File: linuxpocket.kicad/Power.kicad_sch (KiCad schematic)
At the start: 44 parts, among them U1 BQ24295RGER, U2 BQ27426YZFR, U3 TPS63805YFFR, U4 TPS61169DCKR, U5 MT3608L

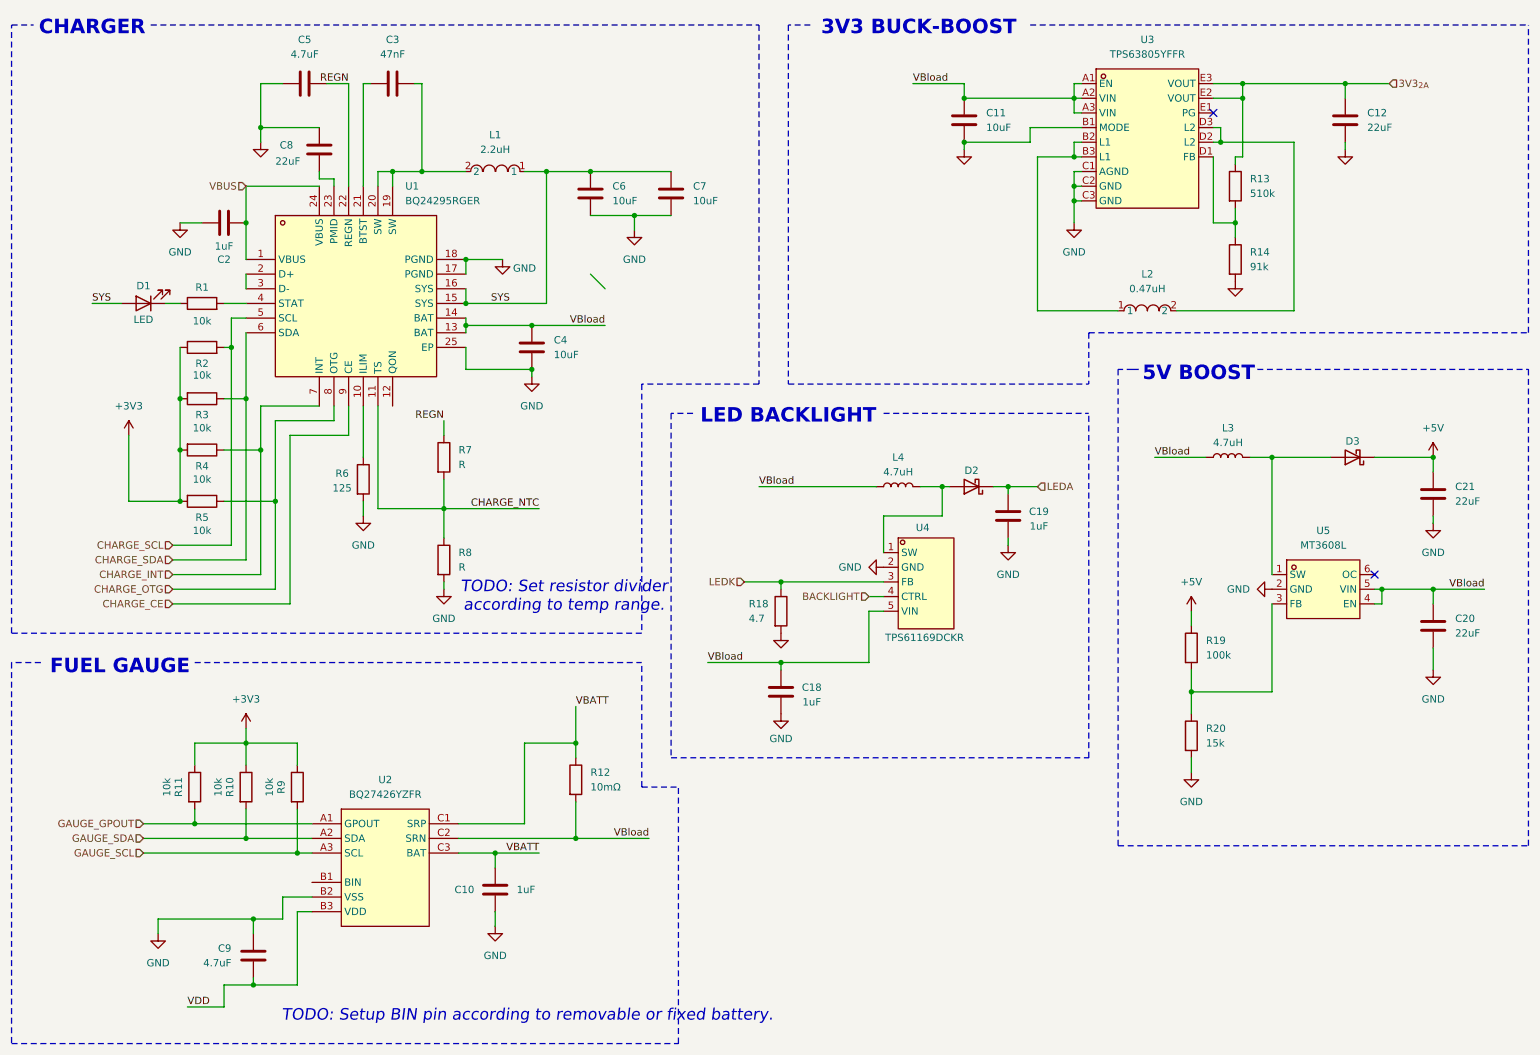
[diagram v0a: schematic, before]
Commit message: Add keyboard, improve many things etc.
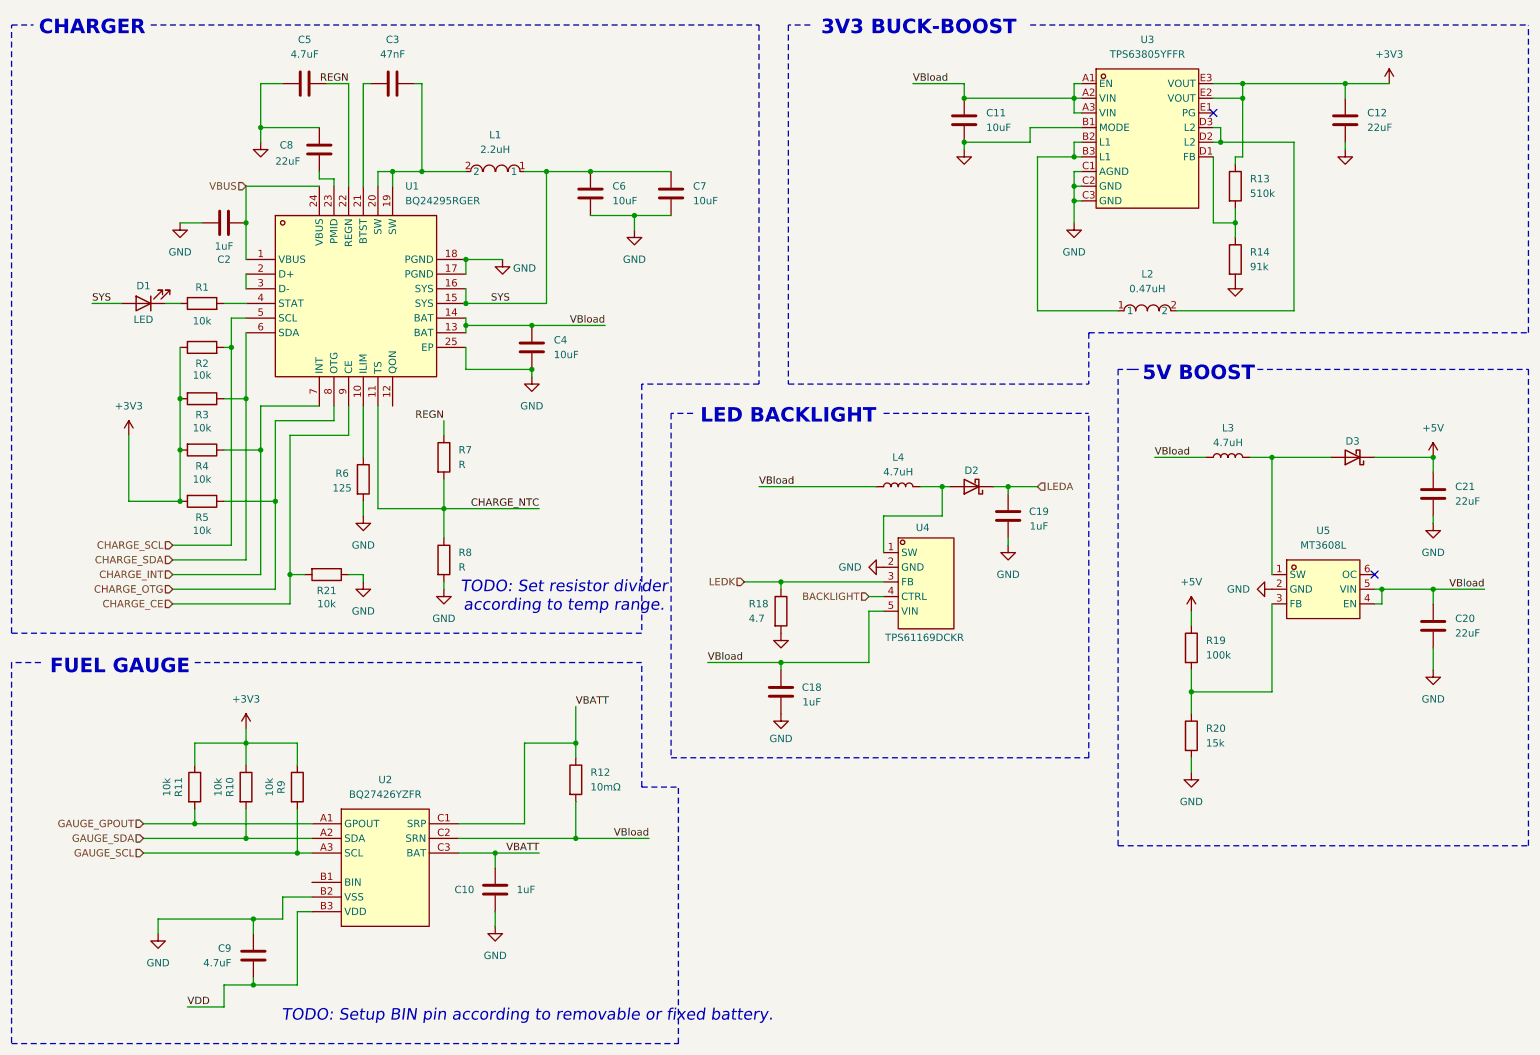
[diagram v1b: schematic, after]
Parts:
- added R21: 10k, symbol Device:R
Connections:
- net 3V3_{2A} is gone; now on net +3V3: C12.1, R13.1, U3.E2 (VOUT), U3.E3 (VOUT)
- net CHARGE_CE: now also R21.2
- net GND: now also R21.1
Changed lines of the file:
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@@
 	)
 	(junction
+		(at 64.77 113.03)
+		(diameter 0)
+		(color 0 0 0 0)
+	)
+	(junction
 		(at 109.22 43.18)
 		(diameter 0)
@@
 		(at 252.73 113.03)
 	)
-	(bus_entry
-		(at 116.84 60.96)
-		(size 2.54 2.54)
-		(stroke
-			(width 0)
-			(type default)
-		)
-	)
 	(wire
 		(pts
@@
 		)
 	)
+	(wire
+		(pts
+			(xy 77.47 113.03) (xy 77.47 114.3)
+		)
+		(stroke
+			(width 0)
+			(type default)
+		)
+	)
 	(polyline
 		(pts
@@
 	(wire
 		(pts
+			(xy 67.31 113.03) (xy 64.77 113.03)
+		)
+		(stroke
+			(width 0)
+			(type default)
+		)
+	)
+	(wire
+		(pts
 			(xy 143.51 114.3) (xy 149.86 114.3)
 		)
@@
 	(wire
 		(pts
-			(xy 64.77 88.9) (xy 64.77 118.11)
+			(xy 64.77 88.9) (xy 64.77 113.03)
 		)
 		(stroke
@@
 	(wire
 		(pts
+			(xy 64.77 113.03) (xy 64.77 118.11)
+		)
+		(stroke
+			(width 0)
+			(type default)
+		)
+	)
+	(wire
+		(pts
 			(xy 201.93 27.94) (xy 200.66 27.94)
 		)
@@
 	(wire
 		(pts
+			(xy 74.93 113.03) (xy 77.47 113.03)
+		)
+		(stroke
+			(width 0)
+			(type default)
+		)
+	)
+	(wire
+		(pts
 			(xy 189.23 106.68) (xy 189.23 107.95)
 		)
@@
 		)
 	)
-	(hierarchical_label "3V3_{2A}"
-		(shape input)
-		(at 255.27 27.94 0)
-		(fields_autoplaced yes)
-		(effects
-			(font
-				(size 1.27 1.27)
-			)
-			(justify left)
-		)
-	)
 	(hierarchical_label "CHARGE_CE"
 		(shape input)
@@
 	)
 	(symbol
+		(lib_id "power:+3V3")
+		(at 255.27 27.94 0)
+		(unit 1)
+		(exclude_from_sim no)
+		(in_bom yes)
+		(on_board yes)
+		(dnp no)
+		(fields_autoplaced yes)
+		(property "Reference" "#PWR04"
+			(at 255.27 31.75 0)
+			(effects
+				(font
+					(size 1.27 1.27)
+				)
+				(hide yes)
+			)
+		)
+		(property "Value" "+3V3"
+			(at 255.27 22.86 0)
+			(effects
+				(font
+					(size 1.27 1.27)
+				)
+			)
+		)
+		(property "Footprint" ""
+			(at 255.27 27.94 0)
+			(effects
+				(font
+					(size 1.27 1.27)
+				)
+				(hide yes)
+			)
+		)
+		(property "Datasheet" ""
+			(at 255.27 27.94 0)
+			(effects
+				(font
+					(size 1.27 1.27)
+				)
+				(hide yes)
+			)
+		)
+		(property "Description" "Power symbol creates a global label with name \"+3V3\""
+			(at 255.27 27.94 0)
+			(effects
+				(font
+					(size 1.27 1.27)
+				)
+				(hide yes)
+			)
+		)
+		(pin "1"
+		)
+		(instances
+			(project "linuxpocket"
+				(path "/de3771bf-b13a-459d-a957-6ff90f7da387/80740467-2537-4aa9-be41-8a76ad0fbd83"
+					(reference "#PWR04")
+					(unit 1)
+				)
+			)
+		)
+	)
+	(symbol
 		(lib_id "power:GND")
 		(at 149.86 123.19 0)
@@
 	(symbol
 		(lib_id "power:GND")
+		(at 77.47 114.3 0)
+		(unit 1)
+		(exclude_from_sim no)
+		(in_bom yes)
+		(on_board yes)
+		(dnp no)
+		(fields_autoplaced yes)
+		(property "Reference" "#PWR047"
+			(at 77.47 120.65 0)
+			(effects
+				(font
+					(size 1.27 1.27)
+				)
+				(hide yes)
+			)
+		)
+		(property "Value" "GND"
+			(at 77.47 119.38 0)
+			(effects
+				(font
+					(size 1.27 1.27)
+				)
+			)
+		)
+		(property "Footprint" ""
+			(at 77.47 114.3 0)
+			(effects
+				(font
+					(size 1.27 1.27)
+				)
+				(hide yes)
+			)
+		)
+		(property "Datasheet" ""
+			(at 77.47 114.3 0)
+			(effects
+				(font
+					(size 1.27 1.27)
+				)
+				(hide yes)
+			)
+		)
+		(property "Description" "Power symbol creates a global label with name \"GND\" , ground"
+			(at 77.47 114.3 0)
+			(effects
+				(font
+					(size 1.27 1.27)
+				)
+				(hide yes)
+			)
+		)
+		(pin "1"
+		)
+		(instances
+			(project "linuxpocket"
+				(path "/de3771bf-b13a-459d-a957-6ff90f7da387/80740467-2537-4aa9-be41-8a76ad0fbd83"
+					(reference "#PWR047")
+					(unit 1)
+				)
+			)
+		)
+	)
+	(symbol
+		(lib_id "power:GND")
 		(at 247.65 39.37 0)
 		(unit 1)
@@
 					(unit 1)
 				)
+			)
+		)
+	)
+	(symbol
+		(lib_id "Device:R")
+		(at 71.12 113.03 270)
+		(unit 1)
+		(exclude_from_sim no)
+		(in_bom yes)
+		(on_board yes)
+		(dnp no)
+		(property "Reference" "R21"
+			(at 71.12 115.824 90)
+			(effects
+				(font
+					(size 1.27 1.27)
+				)
+			)
+		)
+		(property "Value" "10k"
+			(at 71.12 118.11 90)
+			(effects
+				(font
+					(size 1.27 1.27)
+				)
+			)
+		)
+		(property "Footprint" ""
+			(at 71.12 111.252 90)
+			(effects
+				(font
+					(size 1.27 1.27)
+				)
+				(hide yes)
+			)
+		)
+		(property "Datasheet" "~"
+			(at 71.12 113.03 0)
+			(effects
+				(font
+					(size 1.27 1.27)
+				)
+				(hide yes)
+			)
+		)
+		(property "Description" "Resistor"
+			(at 71.12 113.03 0)
+			(effects
+				(font
+					(size 1.27 1.27)
+				)
+				(hide yes)
+			)
+		)
+		(pin "2"
+		)
+		(pin "1"
+		)
+		(instances
+			(project "linuxpocket"
+				(path "/de3771bf-b13a-459d-a957-6ff90f7da387/80740467-2537-4aa9-be41-8a76ad0fbd83"
+					(reference "R21")
+					(unit 1)
+				)

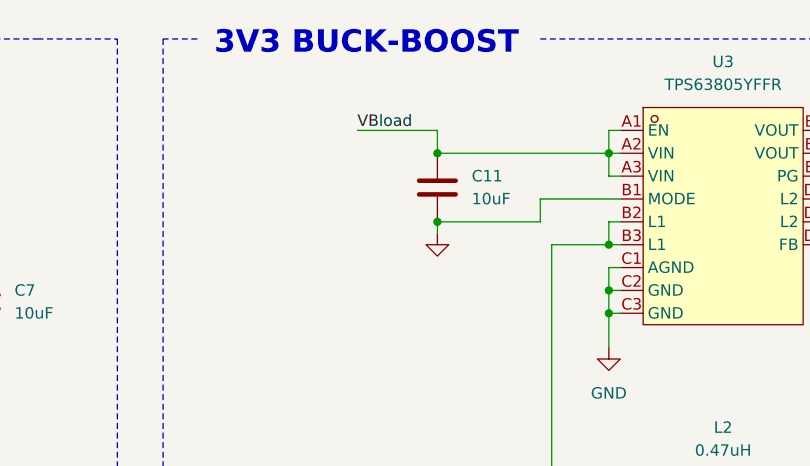
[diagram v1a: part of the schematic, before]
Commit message: Start with HDMI connector.
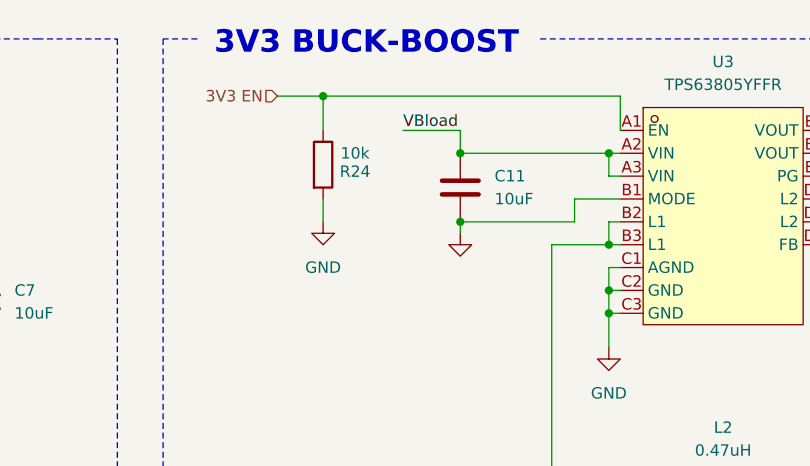
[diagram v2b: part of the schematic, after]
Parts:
- added R24: 10k, symbol Device:R
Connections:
- net GND: now also R24.2
- net VBload: no longer U3.A1 (EN)
- new net 3V3 EN: R24.1, U3.A1 (EN)
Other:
- moved on the sheet: C11

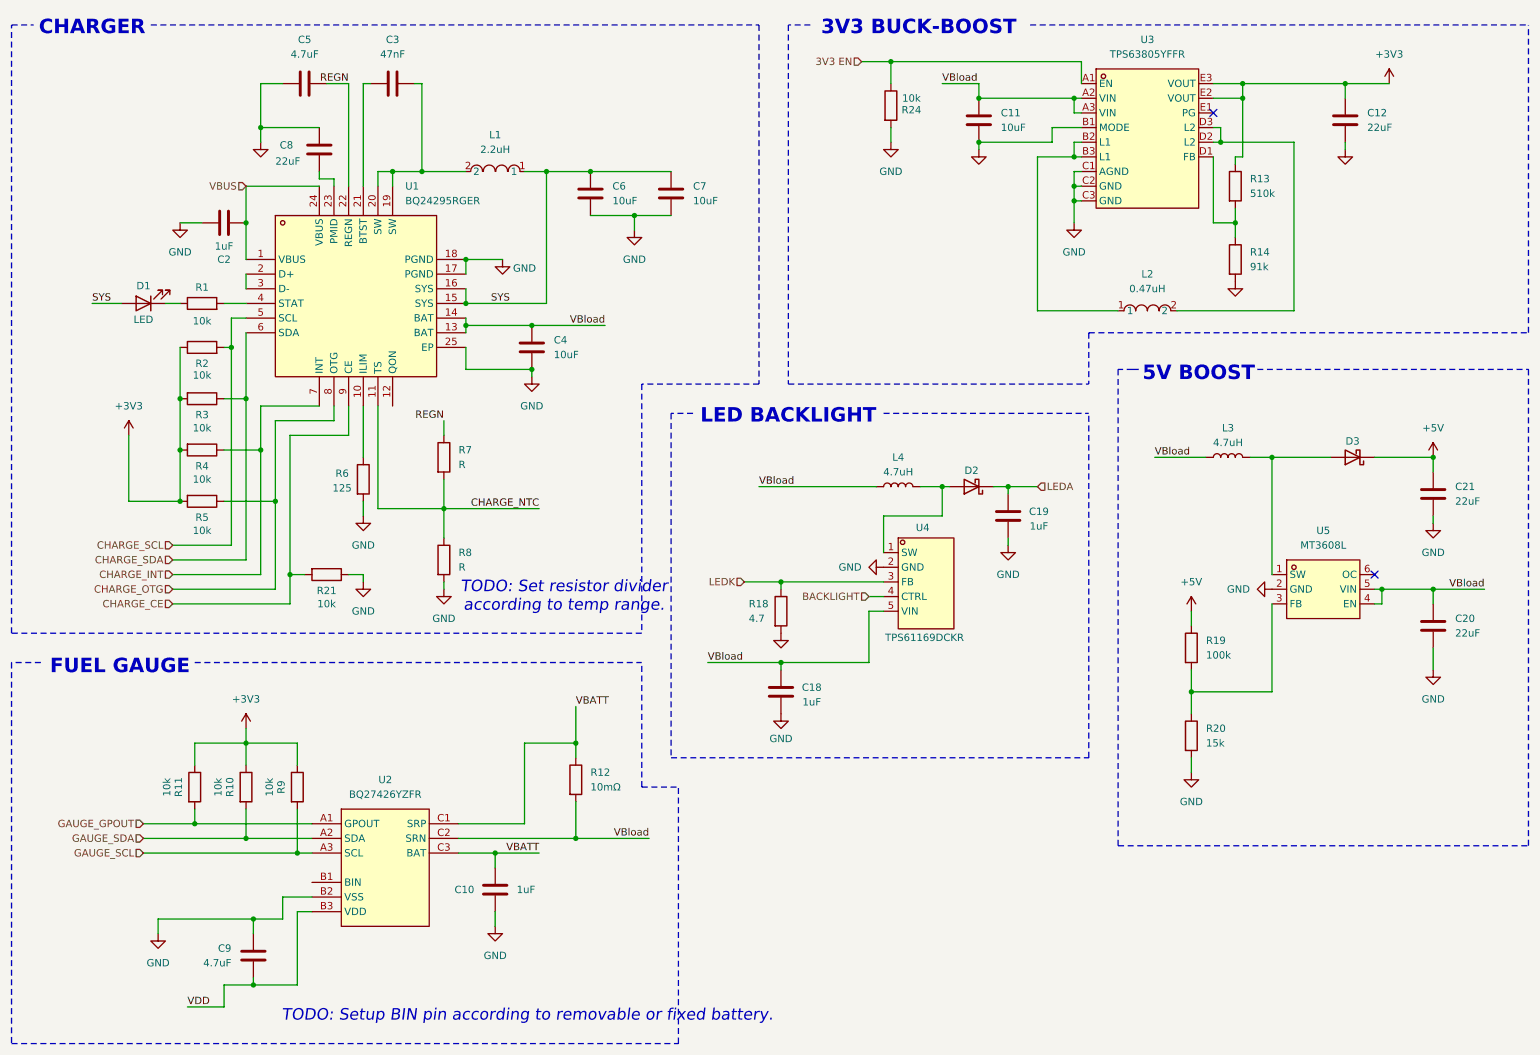
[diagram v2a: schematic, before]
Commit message: Add magnetometer #5. Add footprints to some symbols.
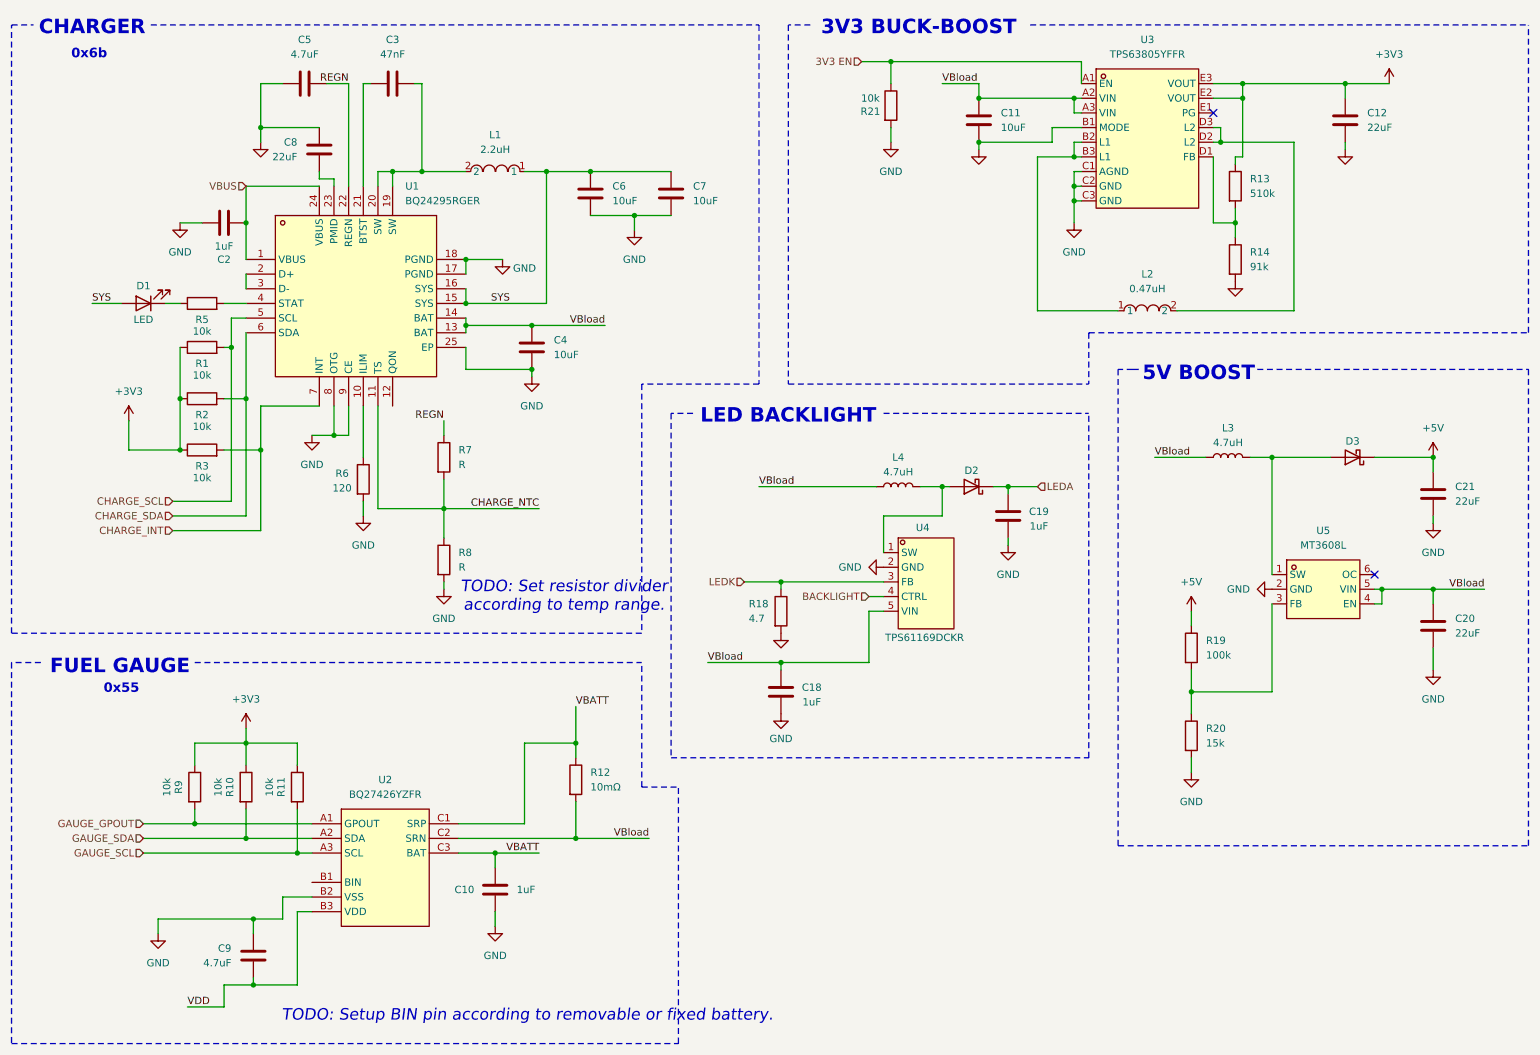
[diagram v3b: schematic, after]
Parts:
- removed R24, R4: 10k, symbol Device:R
- C3: footprint (none) -> Capacitor_SMD:C_0603_1608Metric; LCSC (none) -> C1622
- C5, C9: footprint (none) -> Capacitor_SMD:C_0402_1005Metric; LCSC (none) -> C23733
- C8: footprint (none) -> Capacitor_SMD:C_0603_1608Metric; LCSC (none) -> C59461
- D1: footprint (none) -> Inductor_SMD:L_0603_1608Metric_Pad1.05x0.95mm_HandSolder
- D2: footprint (none) -> Diode_SMD:D_SOD-323; LCSC (none) -> C191023
- D3: footprint (none) -> Diode_SMD:D_SMA; LCSC (none) -> C8678
- R1, R10, R11, R2, R21, R3, R5, R9: footprint (none) -> Resistor_SMD:R_0402_1005Metric; LCSC (none) -> C25744
- R12: footprint (none) -> Resistor_SMD:R_0402_1005Metric; LCSC (none) -> C3024467
- R6: value 125 -> 120; footprint (none) -> Resistor_SMD:R_0402_1005Metric; LCSC (none) -> C25079
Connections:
- net CHARGE_CE is gone; now on net GND: R21.2, U1.9 (CE)
- net +3V3: now also R1.1, R3.1; no longer R3.2, R5.2
- net 3V3 EN: now also R21.1
- net CHARGE_INT: now also R3.2
- net CHARGE_SCL: now also R1.2; no longer R2.2
- net CHARGE_SDA: now also R2.2; no longer R3.1
- net GAUGE_GPOUT: now also R9.2; no longer R11.2
- net GAUGE_SCL: now also R11.2; no longer R9.2
- net GND: now also U1.8 (OTG); no longer R21.1
- net at D1.1 (K): now also R5.1; no longer R1.1
- net at U1.4 (STAT): now also R5.2; no longer R1.2
- removed net CHARGE_OTG: R5.1, U1.8 (OTG)
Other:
- note added: "0x55"
- note added: "0x6b"

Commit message: PCB almost done and schematic finished.
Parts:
- added R16: 10k, Resistor_SMD:R_0402_1005Metric, symbol Device:R
- L3, L4: footprint (none) -> linuxpocket:IND-SMD_L7.1-W6.6_SL0624
- R7: value R -> 15k; footprint (none) -> Resistor_SMD:R_0402_1005Metric; LCSC (none) -> C25756
- R8: value R -> 10k; footprint (none) -> Resistor_SMD:R_0402_1005Metric; LCSC (none) -> C25744
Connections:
- net CHARGE_NTC: now also R7.1, R8.2; no longer R7.2, R8.1
- net GND: now also R7.2, R16.2; no longer R8.2
- net REGN: now also R8.1; no longer R7.1
- net at R5.2: no longer U1.4 (STAT)
- net at U2.B1 (BIN): now also R16.1
- no-connect marks 2 -> 4
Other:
- note removed: "TODO: Set resistor divider according to temp range."
- note removed: "TODO: Setup BIN pin according to removable or fixed battery."
- moved on the sheet: D1, R5
